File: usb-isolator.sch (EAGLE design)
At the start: 17 parts, among them IC1 ADUM3160BRWZ

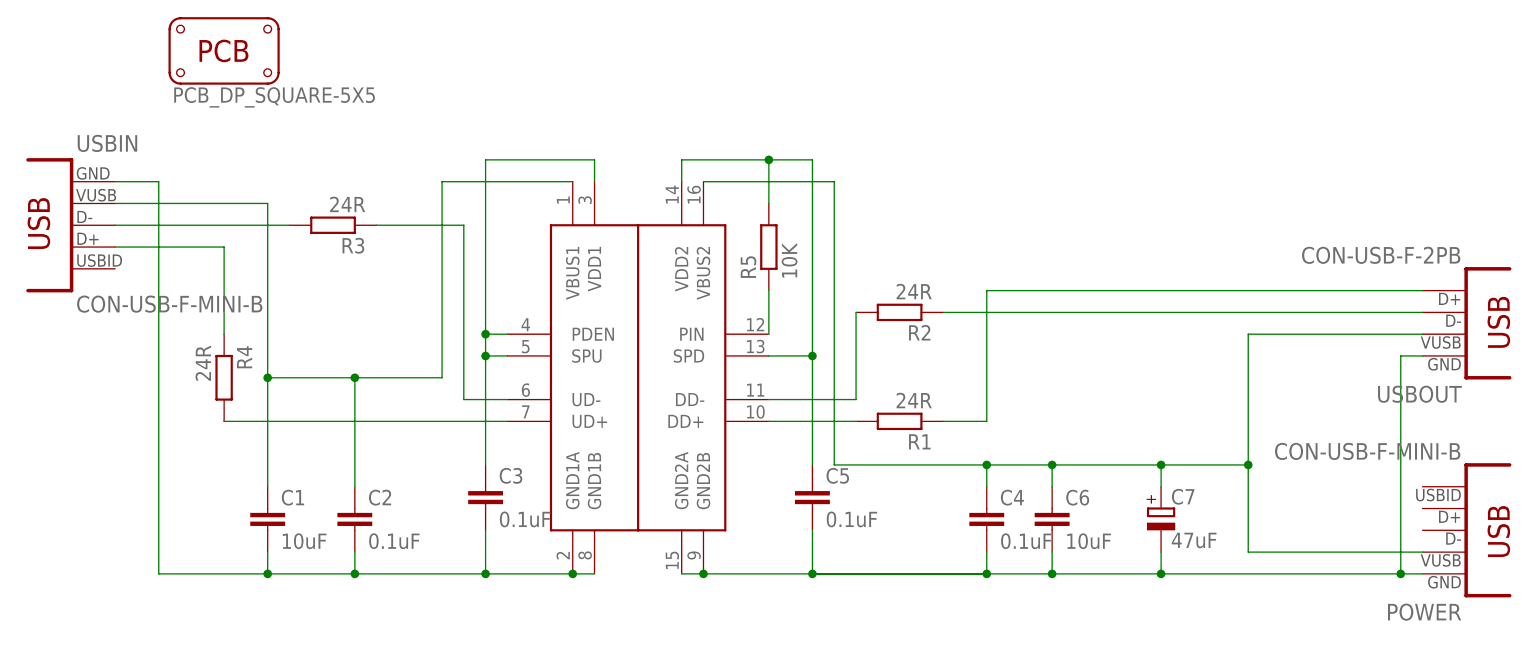
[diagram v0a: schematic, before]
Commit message: Update README, eagle files and schematic image for rev 1.2
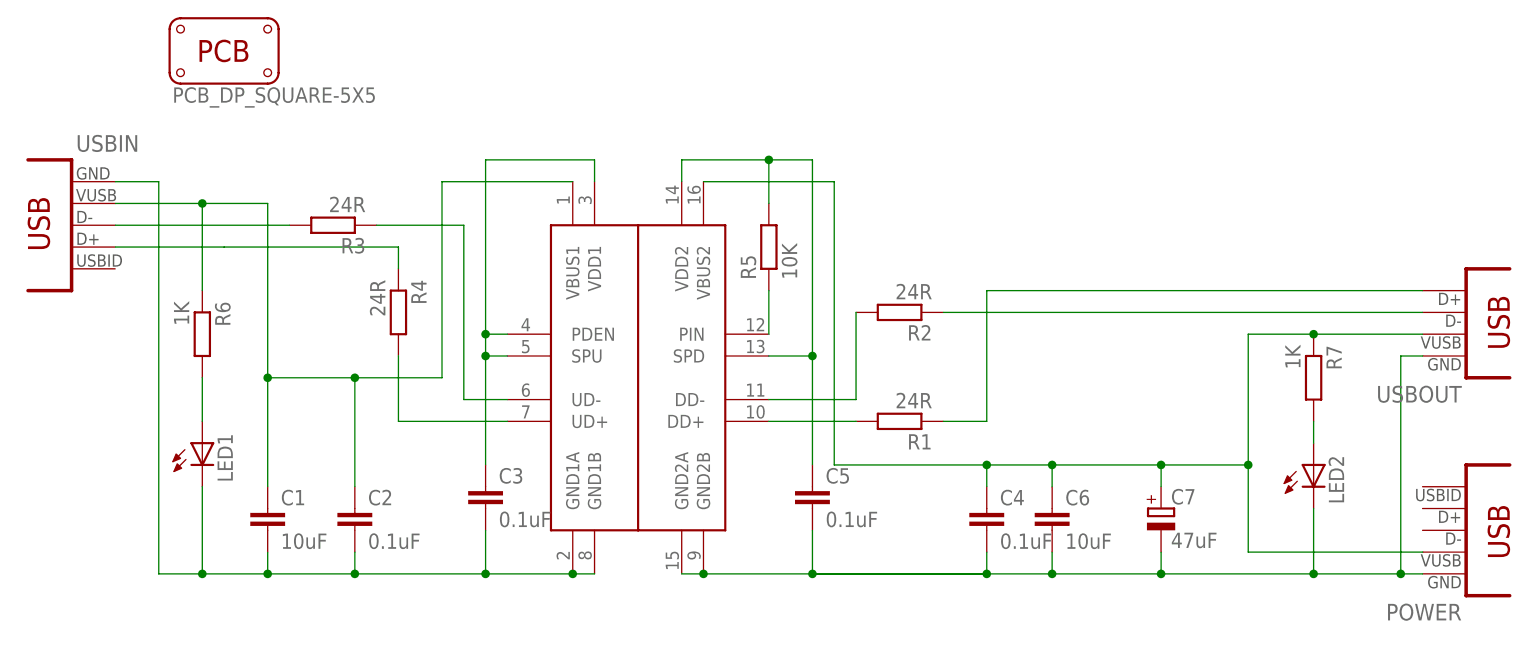
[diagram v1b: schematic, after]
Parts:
- added LED1, LED2: (no value), semiconductors:LED-0805
- added R6, R7: 1K, resistor:R-EU_M0805
- USB-ISOLATOR: device dp_pcb:PCB_DP_SQUARE-5X5 -> mechanical:PCB_DP_SQUARE-5X5
- USBOUT: device dp_devices:CON-USB-F-2PB -> mechanical:CON-USB-F-2PB
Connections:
- new net N$12: LED1.A, R6.2
- new net N$13: LED2.A, R7.2
- net GND1: now also LED1.C
- net GND2: now also LED2.C
- net VBUS1: now also R6.1
- net VBUS2: now also R7.1
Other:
- moved on the sheet: R4
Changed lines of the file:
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@@
 <?xml version="1.0" encoding="utf-8"?>
 <!DOCTYPE eagle SYSTEM "eagle.dtd">
-<eagle version="6.5.0">
+<eagle version="6.6.0">
 <drawing>
 <settings>
@@
 <part name="R5" library="resistor" deviceset="R-EU_" device="M0805" value="10K"/>
 <part name="C7" library="rcl" deviceset="CPOL-EU" device="D/7343-31W" value="47uF"/>
-<part name="USBOUT" library="dp_devices" deviceset="CON-USB-F-2PB" device=""/>
-<part name="USB-ISOLATOR" library="dp_pcb" deviceset="PCB_DP_SQUARE" device="-5X5"/>
+<part name="USBOUT" library="mechanical" deviceset="CON-USB-F-2PB" device=""/>
+<part name="USB-ISOLATOR" library="mechanical" deviceset="PCB_DP_SQUARE" device="-5X5"/>
 <part name="R1" library="resistor" deviceset="R-EU_" device="M0805" value="24R"/>
 <part name="R2" library="resistor" deviceset="R-EU_" device="M0805" value="24R"/>
 <part name="R3" library="resistor" deviceset="R-EU_" device="M0805" value="24R"/>
 <part name="R4" library="resistor" deviceset="R-EU_" device="M0805" value="24R"/>
+<part name="R6" library="resistor" deviceset="R-EU_" device="M0805" value="1K"/>
+<part name="LED1" library="semiconductors" deviceset="LED" device="-0805"/>
+<part name="R7" library="resistor" deviceset="R-EU_" device="M0805" value="1K"/>
+<part name="LED2" library="semiconductors" deviceset="LED" device="-0805"/>
 </parts>
 <sheets>
@@
 <instances>
 <instance part="IC1" gate="G$1" x="76.2" y="53.34"/>
-<instance part="USBIN" gate="USB" x="12.7" y="68.58"/>
-<instance part="POWER" gate="USB" x="175.26" y="33.02" rot="R180"/>
+<instance part="USBIN" gate="USB" x="12.7" y="68.58" smashed="yes">
+<attribute name="NAME" x="13.208" y="77.1525" size="1.9304" layer="95"/>
+</instance>
+<instance part="POWER" gate="USB" x="175.26" y="33.02" smashed="yes" rot="R180">
+<attribute name="NAME" x="174.752" y="24.4475" size="1.9304" layer="95" rot="R180"/>
+</instance>
 <instance part="C4" gate="G$1" x="119.38" y="35.56"/>
 <instance part="C6" gate="G$1" x="127" y="35.56"/>
@@
 <instance part="R5" gate="G$1" x="93.98" y="66.04" rot="R90"/>
 <instance part="C7" gate="G$1" x="139.7" y="35.56"/>
-<instance part="USBOUT" gate="USB" x="175.26" y="58.42" rot="R180"/>
+<instance part="USBOUT" gate="USB" x="175.26" y="58.42" smashed="yes" rot="R180">
+<attribute name="NAME" x="174.752" y="49.8475" size="1.9304" layer="95" rot="R180"/>
+</instance>
 <instance part="USB-ISOLATOR" gate="G$1" x="30.48" y="88.9"/>
 <instance part="R1" gate="G$1" x="109.22" y="45.72" rot="R180"/>
 <instance part="R2" gate="G$1" x="109.22" y="58.42" rot="R180"/>
 <instance part="R3" gate="G$1" x="43.18" y="68.58" rot="R180"/>
-<instance part="R4" gate="G$1" x="30.48" y="50.8" rot="R270"/>
+<instance part="R4" gate="G$1" x="50.8" y="58.42" rot="R270"/>
+<instance part="R6" gate="G$1" x="27.94" y="55.88" rot="R270"/>
+<instance part="LED1" gate="LED" x="27.94" y="43.18"/>
+<instance part="R7" gate="G$1" x="157.48" y="50.8" rot="R270"/>
+<instance part="LED2" gate="LED" x="157.48" y="40.64"/>
 </instances>
 <busses>
@@
 <wire x1="22.86" y1="73.66" x2="22.86" y2="27.94" width="0.1524" layer="91"/>
 <pinref part="IC1" gate="G$1" pin="GND1A"/>
-<wire x1="22.86" y1="27.94" x2="35.56" y2="27.94" width="0.1524" layer="91"/>
+<wire x1="22.86" y1="27.94" x2="27.94" y2="27.94" width="0.1524" layer="91"/>
 <pinref part="IC1" gate="G$1" pin="GND1B"/>
+<wire x1="27.94" y1="27.94" x2="35.56" y2="27.94" width="0.1524" layer="91"/>
 <wire x1="35.56" y1="27.94" x2="45.72" y2="27.94" width="0.1524" layer="91"/>
 <wire x1="45.72" y1="27.94" x2="60.96" y2="27.94" width="0.1524" layer="91"/>
@@
 <wire x1="45.72" y1="30.48" x2="45.72" y2="27.94" width="0.1524" layer="91"/>
 <junction x="45.72" y="27.94"/>
+<pinref part="LED1" gate="LED" pin="C"/>
+<wire x1="27.94" y1="38.1" x2="27.94" y2="27.94" width="0.1524" layer="91"/>
+<junction x="27.94" y="27.94"/>
 </segment>
 </net>
@@
 <pinref part="IC1" gate="G$1" pin="GND2B"/>
 <junction x="86.36" y="27.94"/>
-<wire x1="167.64" y1="27.94" x2="139.7" y2="27.94" width="0.1524" layer="91"/>
+<wire x1="167.64" y1="27.94" x2="157.48" y2="27.94" width="0.1524" layer="91"/>
+<wire x1="157.48" y1="27.94" x2="139.7" y2="27.94" width="0.1524" layer="91"/>
 <wire x1="139.7" y1="27.94" x2="127" y2="27.94" width="0.1524" layer="91"/>
 <wire x1="127" y1="27.94" x2="119.38" y2="27.94" width="0.1524" layer="91"/>
@@
 <wire x1="167.64" y1="53.34" x2="167.64" y2="27.94" width="0.1524" layer="91"/>
 <junction x="167.64" y="27.94"/>
+<pinref part="LED2" gate="LED" pin="C"/>
+<wire x1="157.48" y1="35.56" x2="157.48" y2="27.94" width="0.1524" layer="91"/>
+<junction x="157.48" y="27.94"/>
 </segment>
 </net>
@@
 <junction x="139.7" y="40.64"/>
 <pinref part="USBOUT" gate="USB" pin="VUSB"/>
-<wire x1="170.18" y1="55.88" x2="149.86" y2="55.88" width="0.1524" layer="91"/>
+<wire x1="170.18" y1="55.88" x2="157.48" y2="55.88" width="0.1524" layer="91"/>
+<wire x1="157.48" y1="55.88" x2="149.86" y2="55.88" width="0.1524" layer="91"/>
 <wire x1="149.86" y1="55.88" x2="149.86" y2="40.64" width="0.1524" layer="91"/>
 <junction x="149.86" y="40.64"/>
+<pinref part="R7" gate="G$1" pin="1"/>
+<junction x="157.48" y="55.88"/>
 </segment>
 </net>
@@
 <segment>
 <pinref part="USBIN" gate="USB" pin="VUSB"/>
-<wire x1="17.78" y1="71.12" x2="35.56" y2="71.12" width="0.1524" layer="91"/>
+<wire x1="17.78" y1="71.12" x2="27.94" y2="71.12" width="0.1524" layer="91"/>
+<wire x1="27.94" y1="71.12" x2="35.56" y2="71.12" width="0.1524" layer="91"/>
 <wire x1="35.56" y1="71.12" x2="35.56" y2="50.8" width="0.1524" layer="91"/>
 <wire x1="35.56" y1="50.8" x2="45.72" y2="50.8" width="0.1524" layer="91"/>
@@
 <wire x1="45.72" y1="38.1" x2="45.72" y2="50.8" width="0.1524" layer="91"/>
 <junction x="45.72" y="50.8"/>
+<pinref part="R6" gate="G$1" pin="1"/>
+<wire x1="27.94" y1="71.12" x2="27.94" y2="60.96" width="0.1524" layer="91"/>
+<junction x="27.94" y="71.12"/>
 </segment>
 </net>
@@
 <wire x1="17.78" y1="66.04" x2="30.48" y2="66.04" width="0.1524" layer="91"/>
 <pinref part="R4" gate="G$1" pin="1"/>
-<wire x1="30.48" y1="66.04" x2="30.48" y2="55.88" width="0.1524" layer="91"/>
+<wire x1="30.48" y1="66.04" x2="50.8" y2="66.04" width="0.1524" layer="91"/>
+<wire x1="50.8" y1="66.04" x2="50.8" y2="63.5" width="0.1524" layer="91"/>
 </segment>
 </net>
@@
 <pinref part="R4" gate="G$1" pin="2"/>
 <pinref part="IC1" gate="G$1" pin="UD+"/>
-<wire x1="30.48" y1="45.72" x2="63.5" y2="45.72" width="0.1524" layer="91"/>
+<wire x1="50.8" y1="53.34" x2="50.8" y2="45.72" width="0.1524" layer="91"/>
+<wire x1="50.8" y1="45.72" x2="63.5" y2="45.72" width="0.1524" layer="91"/>
 </segment>
 </net>
@@
 </segment>
 </net>
+<net name="N$12" class="0">
+<segment>
+<pinref part="R6" gate="G$1" pin="2"/>
+<pinref part="LED1" gate="LED" pin="A"/>
+<wire x1="27.94" y1="50.8" x2="27.94" y2="45.72" width="0.1524" layer="91"/>
+</segment>
+</net>
+<net name="N$13" class="0">
+<segment>
+<pinref part="R7" gate="G$1" pin="2"/>
+<pinref part="LED2" gate="LED" pin="A"/>
+<wire x1="157.48" y1="45.72" x2="157.48" y2="43.18" width="0.1524" layer="91"/>
+</segment>
+</net>
 </nets>
 </sheet>
 </sheets>
-<errors>
-</errors>
 </schematic>
 </drawing>
